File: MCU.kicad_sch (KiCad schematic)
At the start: 6 parts, among them U2 STM32G431CBU6, U3 TCAN337, Y1 ECS-80-20-5PX-TR

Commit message: MCU schematics update
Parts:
- removed U3: TCAN337, symbol Interface_CAN_LIN:TCAN337
- added C18, C19: 33pF, symbol Device:C_Small
- added C20: 100nF, Capacitor_SMD:C_0402_1005Metric, symbol Device:C_Small
- added C21: 1uF, Capacitor_SMD:C_0603_1608Metric, symbol Device:C
- added C22, C36: 4u7, Capacitor_SMD:C_0603_1608Metric, symbol Device:C_Small
- added C23, C24, C25, C26, C27, C32, C35, C37, C38, C39: 100n, Capacitor_SMD:C_0402_1005Metric, symbol Device:C_Small
- added C28, C42: 1u, Capacitor_SMD:C_0402_1005Metric, symbol Device:C_Small
- added C29, C43: 10n, Capacitor_SMD:C_0402_1005Metric, symbol Device:C_Small
- added C30, C31: 12p, Capacitor_SMD:C_0402_1005Metric, symbol Device:C_Small
- added C33, C34: 2u2, Capacitor_SMD:C_0603_1608Metric, symbol Device:C_Small
- added D9: ESD7104MUTAG, ESD8104MUTAG, symbol ESD7104MUTAG:ESD7104MUTAG
- added IC3: TCAN330DCNT, lib:SOT65P280X145-8N, symbol lib:TCAN330DCNT
- added J1: SM04B-GHS-TB, lib:CONN_SM04B-GHS-TB_JST, symbol lib:SM04B-GHS-TB
- added J2: Conn_01x04_Pin, Connector_PinHeader_1.00mm:PinHeader_1x04_P1.00mm_Vertical, symbol Connector:Conn_01x04_Pin
- added J3: USB_C_Receptacle_USB2.0_16P, Connector_USB:USB_C_Receptacle_GCT_USB4105-xx-A_16P_TopMnt_Horizontal, symbol Connector:USB_C_Receptacle_USB2.0_16P
- added L2: 39n, Inductor_SMD:L_0402_1005Metric, symbol Device:L_Small
- added L3: 100MHz / 1kR, Inductor_SMD:L_0402_1005Metric, symbol Device:L_Small
- added R18, R20: 10k, Resistor_SMD:R_0402_1005Metric, symbol Device:R_Small
- added R19: 120R, Resistor_SMD:R_0402_1005Metric, symbol Device:R_Small
- added R21: 47, Resistor_SMD:R_0402_1005Metric, symbol Device:R_Small
- added R22, R23: 2k2, Resistor_SMD:R_0402_1005Metric, symbol Device:R_Small
- added SW1: SW_SPDT, Button_Switch_SMD:SW_SPDT_PCM12, symbol Switch:SW_SPDT
- added U7: STM32F407VGTx, Package_QFP:LQFP-100_14x14mm_P0.5mm, symbol MCU_ST_STM32F4:STM32F407VGTx
- added Y2: 16MHz, Crystal:Crystal_SMD_3225-4Pin_3.2x2.5mm, symbol Device:Crystal_GND24_Small
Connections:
- net VDD is gone; now on net +3.3V: U2.23 (VDD), U2.35 (VDD), U2.48 (VDD)
- net GND: now also U2.49 (VSS), C18.2, C19.2, C20.2, C21.2, C22.2, C23.2, C24.2, C25.2, C26.2, C27.2, C28.2, C29.2, C30.2, C31.2, C32.2, C33.2, C34.2, C35.2, C36.2, C37.2, C38.2, C39.2, C42.2, C43.2, D9.3 (GND_1), D9.8 (GND_2), IC3.2 (GND), J1.3, J1.4, J2.4 (Pin_4), J3.A1 (GND), J3.A12 (GND), J3.B1 (GND), J3.B12 (GND), J3.S1 (SHIELD), SW1.3 (C), U7.10 (VSS), U7.20 (VSSA), U7.27 (VSS), U7.74 (VSS), U7.99 (VSS), Y2.2, Y2.4
- net at Y1.1: now also U2.6 (PF1-OSC_OUT), C18.1
- net at Y1.2: now also U2.5 (PF0-OSC_IN), C19.1
- net +3.3V: now reaches U2.1 (VBAT)
- net +3.3V: now also C20.1, C22.1, C23.1, C24.1, C25.1, C26.1, C27.1, C36.1, C37.1, C38.1, C39.1, IC3.3 (VCC), J2.1 (Pin_1), L2.1, L3.1, R22.1, R23.1, SW1.1 (A), U7.100 (VDD), U7.11 (VDD), U7.19 (VDD), U7.28 (VDD), U7.50 (VDD), U7.6 (VBAT), U7.75 (VDD)
- net SENS3: now reaches U2.10 (PA2)
- net INLB: now reaches U2.17 (PB0)
- net INLC: now reaches U2.18 (PB1)
- net INLA: now reaches U2.2 (PC13)
- net +3.3VA: now reaches U2.20 (VREF+)
- net +3.3VA: now also U2.21 (VDDA), C28.1, C29.1, C32.1, C35.1, C42.1, C43.1, L2.2, L3.2, U7.21 (VREF+), U7.22 (VDDA)
- net INHA: now reaches U2.30 (PA8)
- net INHB: now reaches U2.31 (PA9)
- net INHC: now reaches U2.32 (PA10)
- net USB_DN: now reaches U2.33 (PA11)
- net USB_DN: now also D9.2 (IO_2), D9.6 (NC_1), J3.A7 (D-), J3.B7 (D-)
- net USB_DP: now reaches U2.34 (PA12)
- net USB_DP: now also D9.1 (IO_1), D9.7 (NC_2), J3.A6 (D+), J3.B6 (D+)
- net SWDIO: now reaches U2.36 (PA13)
- net SWDIO: now also J2.2 (Pin_2), U7.72 (PA13)
- net SWCLK: now reaches U2.37 (PA14)
- net SWCLK: now also J2.3 (Pin_3), U7.76 (PA14)
- net UART_N: now reaches U2.39 (PC10)
- net UART_N: now also IC3.4 (RXD)
- net UART_P: now reaches U2.40 (PC11)
- net UART_P: now also IC3.1 (TXD)
- net BOOT0: now reaches U2.46 (PB8-BOOT0)
- net BOOT0: now also R20.2, U7.94 (BOOT0)
- net SENS1: now reaches U2.8 (PA0)
- net SENS2: now reaches U2.9 (PA1)
- new net: R20.1, SW1.2 (B)
- new net: IC3.6 (CANL), J1.1, R19.1
- new net: IC3.7 (CANH), J1.2, R19.2
- new net: C34.1, U7.49 (VCAP_1)
- new net: C33.1, U7.73 (VCAP_2)
- new net: IC3.5 (SHDN), R18.1
- new net: C31.1, R21.2, Y2.3
- new net BLUE_LED: U7.29 (PA4)
- new net GREEN_LED: U7.26 (PA3)
- new net HSE_IN: C30.1, U7.12 (PH0), Y2.1
- new net HSE_OUT: R21.1, U7.13 (PH1)
- new net I2C1_SCL: R22.2, U7.63 (PC6)
- new net I2C1_SDA: R23.2, U7.64 (PC7)
- new net NRST: U7.14 (NRST)
- new net PD2: IC3.8 (S), R18.2
- new net RED_LED: U7.25 (PA2)
- new net SWO: U7.89 (PB3)
- new net USART3_RX: U7.79 (PC11)
- new net USART3_TX: U7.78 (PC10)
- new net USB_D+: U7.71 (PA12)
- new net USB_D-: U7.70 (PA11)
- new net VBUS: C21.1, D9.4 (IO_3), D9.9 (NC_3), J3.A4 (VBUS), J3.A9 (VBUS), J3.B4 (VBUS), J3.B9 (VBUS)
- no-connect marks 0 -> 40
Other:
- note added: "Cload = 2 * (CL - Cstray)"
- note added: "STM32 Microcontroller"
- note added: "a 16 MHz crystal is perfectly fine for an STM32F407 and for USB Full-Speed, as long as you run the PLL to generate the 48 MHz USB clock and a stable SYSCLK."
- note added: "https://jlcpcb.com/partdetail/Korean_HropartsElec-TF01A/C91145"
- moved on the sheet: Y1

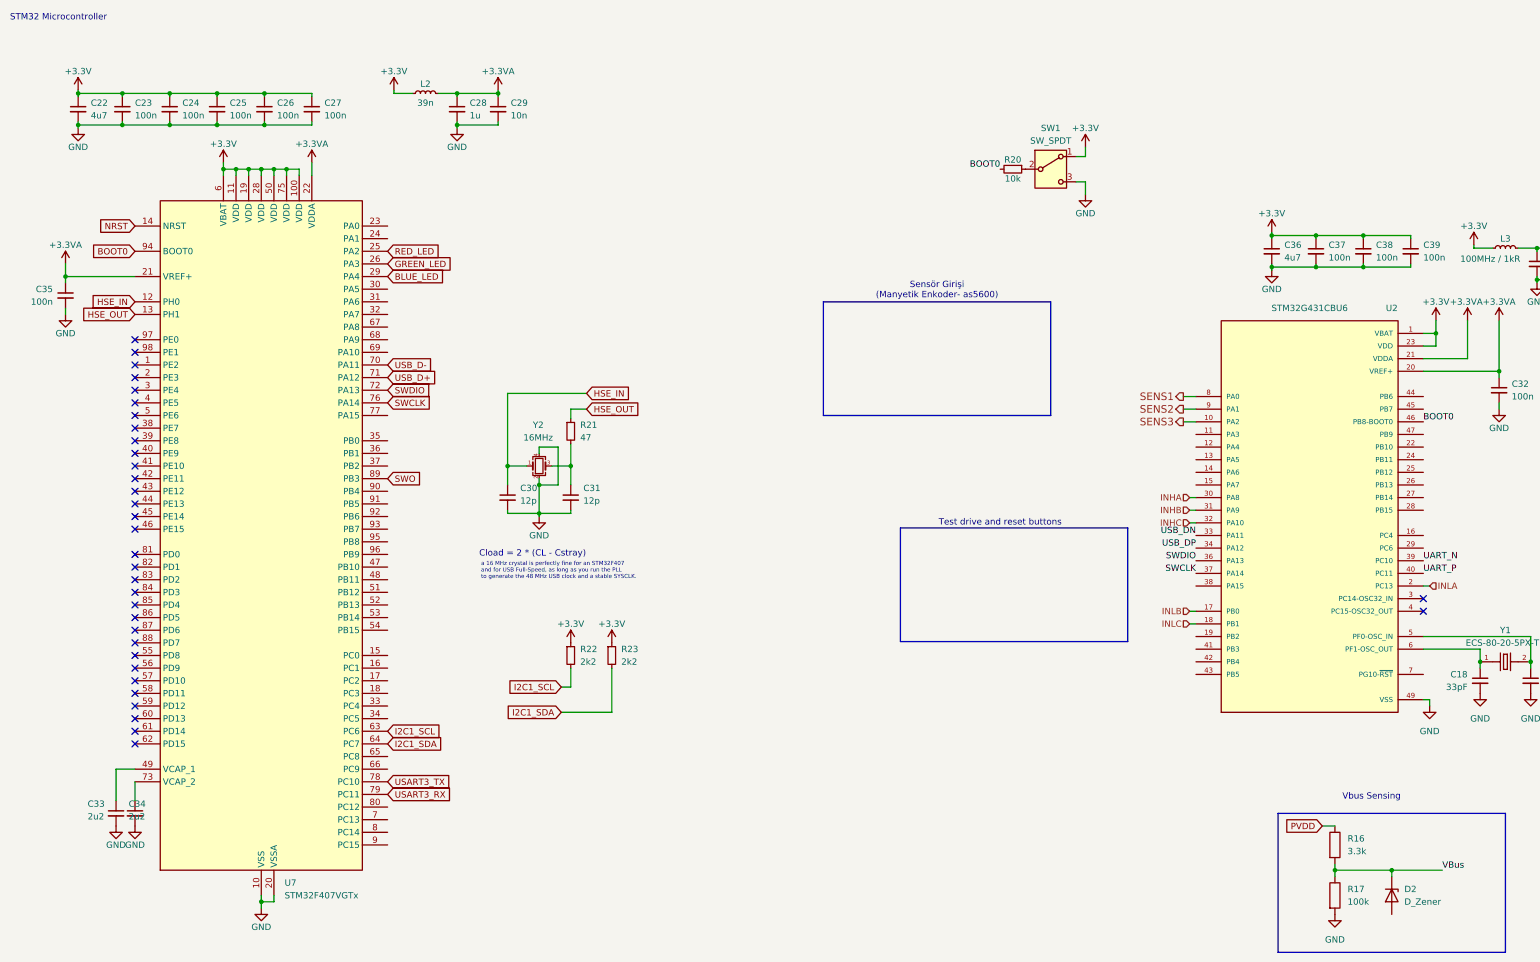
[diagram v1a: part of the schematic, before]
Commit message: MCU schematics update
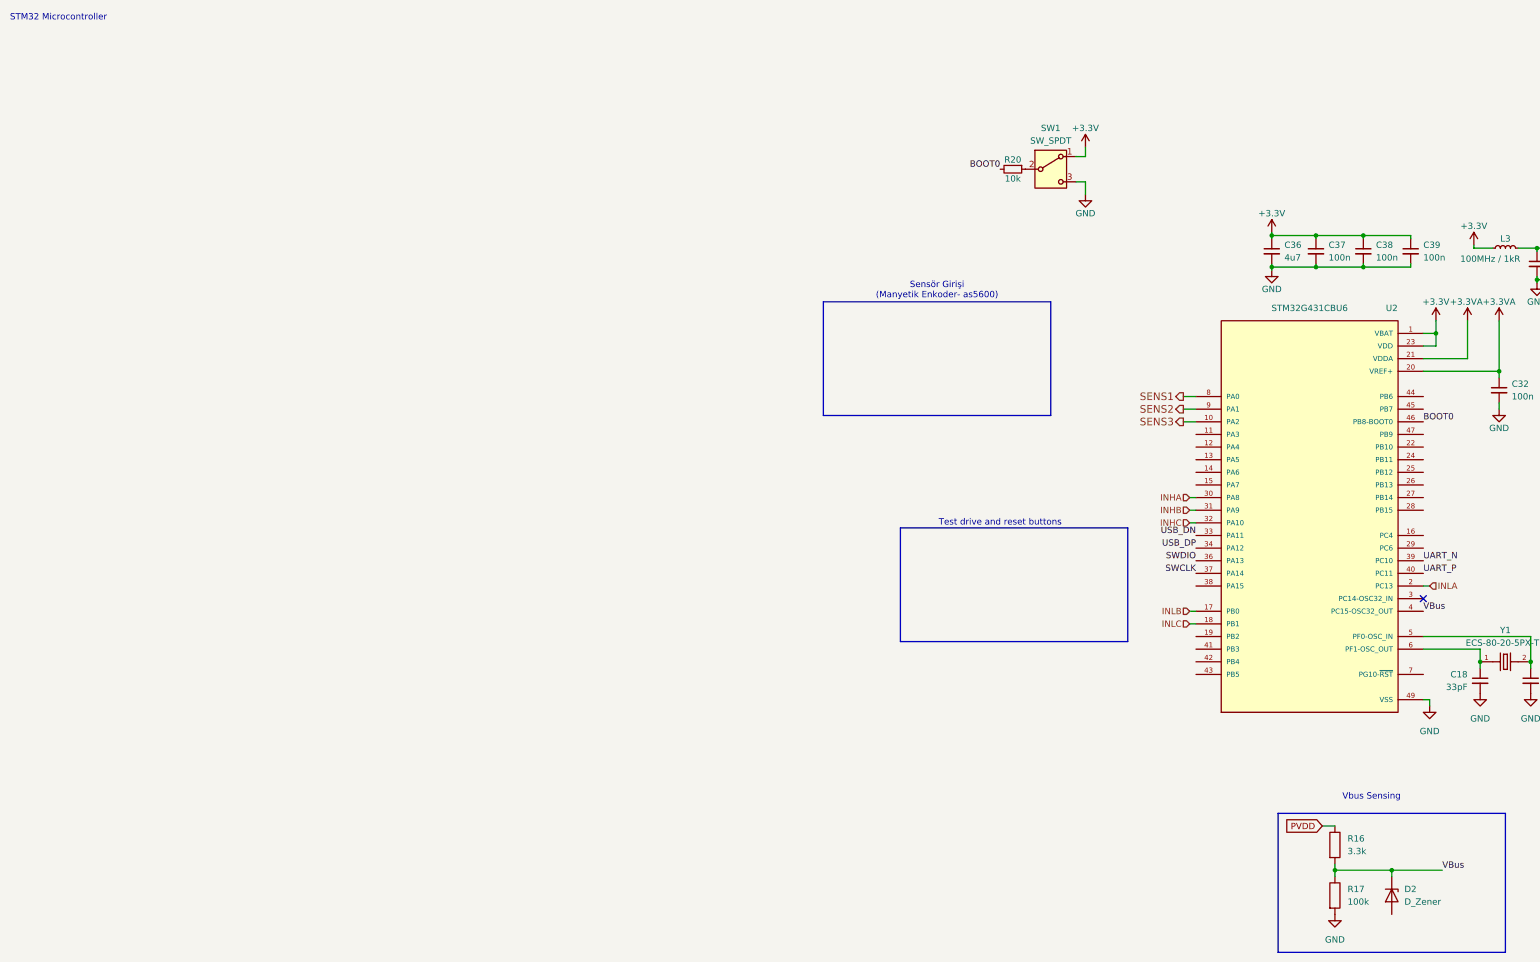
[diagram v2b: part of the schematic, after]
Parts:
- removed C22: 4u7, Capacitor_SMD:C_0603_1608Metric, symbol Device:C_Small
- removed C23, C24, C25, C26, C27, C35: 100n, Capacitor_SMD:C_0402_1005Metric, symbol Device:C_Small
- removed C28: 1u, Capacitor_SMD:C_0402_1005Metric, symbol Device:C_Small
- removed C29: 10n, Capacitor_SMD:C_0402_1005Metric, symbol Device:C_Small
- removed C30, C31: 12p, Capacitor_SMD:C_0402_1005Metric, symbol Device:C_Small
- removed C33, C34: 2u2, Capacitor_SMD:C_0603_1608Metric, symbol Device:C_Small
- removed L2: 39n, Inductor_SMD:L_0402_1005Metric, symbol Device:L_Small
- removed R21: 47, Resistor_SMD:R_0402_1005Metric, symbol Device:R_Small
- removed R22, R23: 2k2, Resistor_SMD:R_0402_1005Metric, symbol Device:R_Small
- removed U7: STM32F407VGTx, Package_QFP:LQFP-100_14x14mm_P0.5mm, symbol MCU_ST_STM32F4:STM32F407VGTx
- removed Y2: 16MHz, Crystal:Crystal_SMD_3225-4Pin_3.2x2.5mm, symbol Device:Crystal_GND24_Small
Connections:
- net VBus: now also U2.4 (PC15-OSC32_OUT)
- no-connect marks 40 -> 7
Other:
- note removed: "Cload = 2 * (CL - Cstray)"
- note removed: "a 16 MHz crystal is perfectly fine for an STM32F407 and for USB Full-Speed, as long as you run the PLL to generate the 48 MHz USB clock and a stable SYSCLK."

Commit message: whakkjls
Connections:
- net GND: now also D2.2 (A)
- net VBus: now also U2.19 (PB2); no longer U2.4 (PC15-OSC32_OUT)
- net I2C1_SCL: now reaches U2.38 (PA15)
- net I2C1_SDA: now reaches U2.45 (PB7)
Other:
- moved on the sheet: D2, J2, R16, R17, R20, SW1

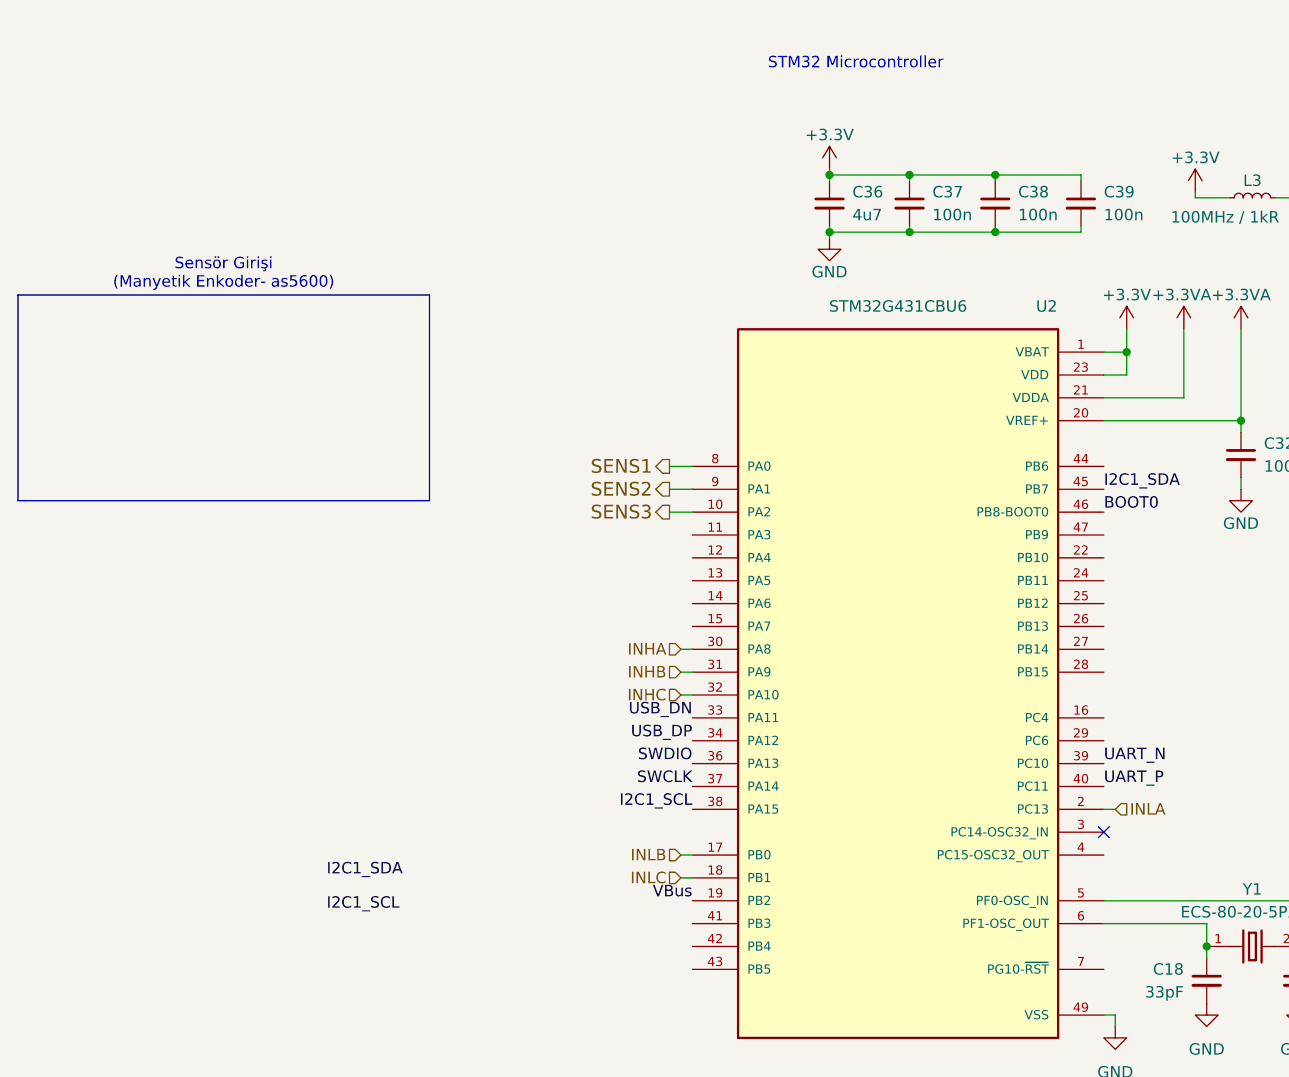
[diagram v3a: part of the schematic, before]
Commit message: some pins changes"
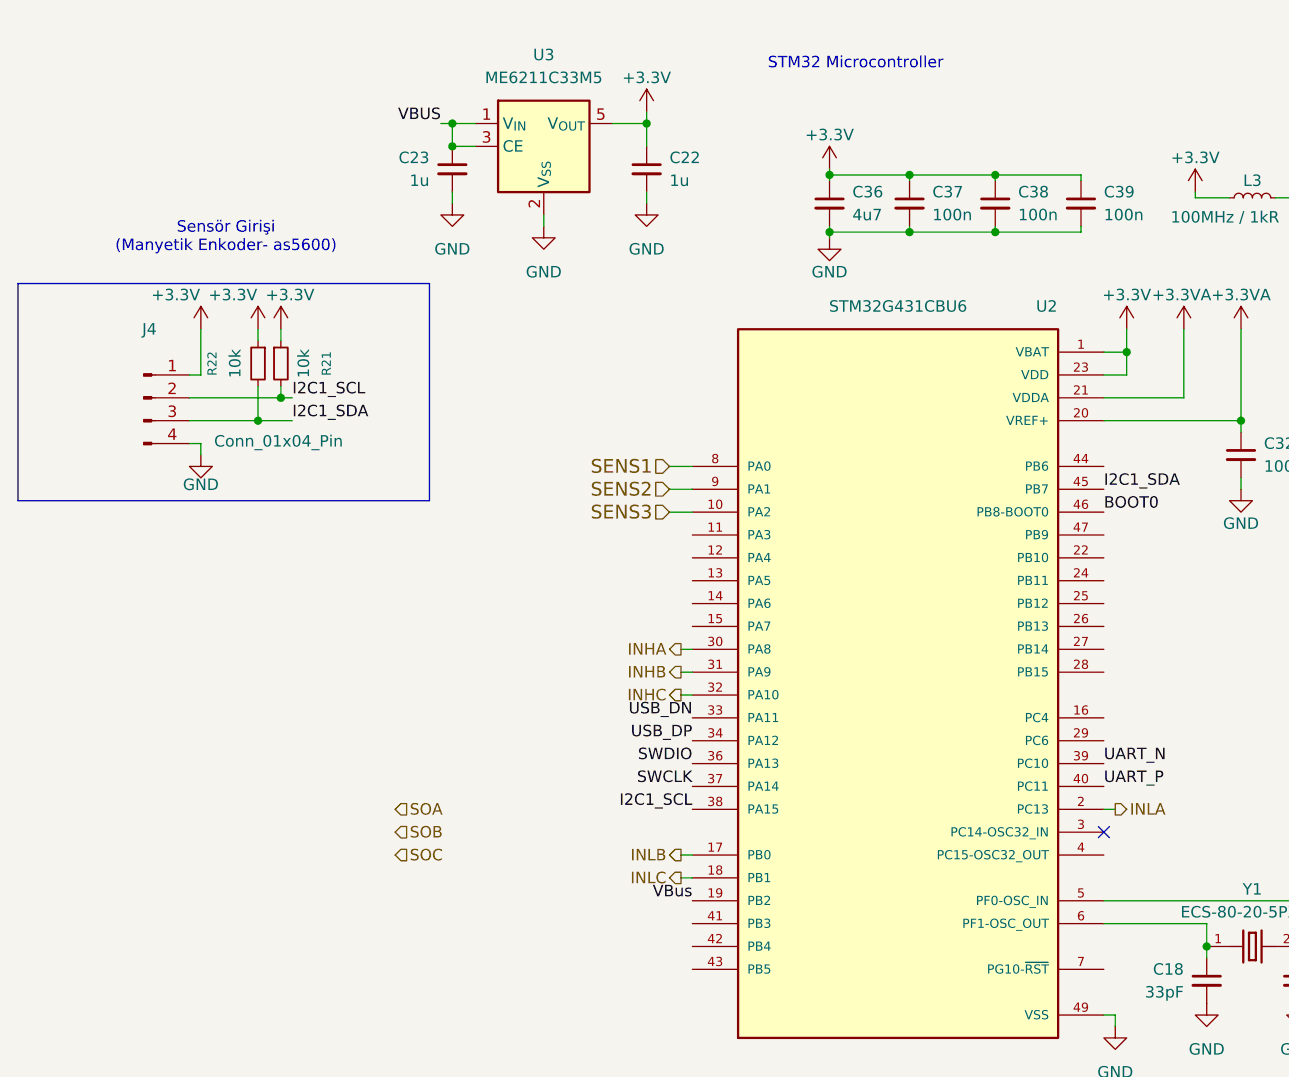
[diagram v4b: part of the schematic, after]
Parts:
- added C22, C23: 1u, Capacitor_SMD:C_0402_1005Metric, symbol Device:C_Small
- added J4: Conn_01x04_Pin, symbol Connector:Conn_01x04_Pin
- added R21, R22: 10k, Resistor_SMD:R_0402_1005Metric, symbol Device:R_Small
- added U3: ME6211C33M5, Package_TO_SOT_SMD:SOT-23-5, symbol Regulator_Linear:ME6211C33M5
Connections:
- net +3.3V: now also C22.1, J4.1 (Pin_1), R21.1, R22.1, U3.5 (V_{OUT})
- net GND: now also C22.2, C23.2, J4.4 (Pin_4), U3.2 (V_{SS})
- net I2C1_SCL: now also J4.2 (Pin_2), R21.2
- net I2C1_SDA: now also J4.3 (Pin_3), R22.2
- net VBUS: now also C23.1, U3.1 (V_{IN}), U3.3 (CE)

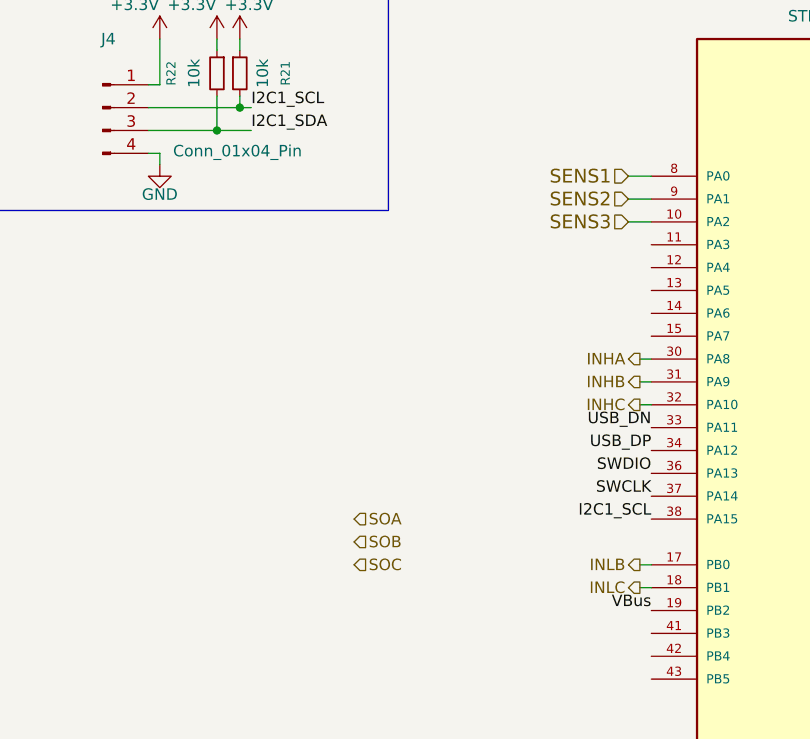
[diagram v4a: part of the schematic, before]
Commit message: current sense -> bemf switch
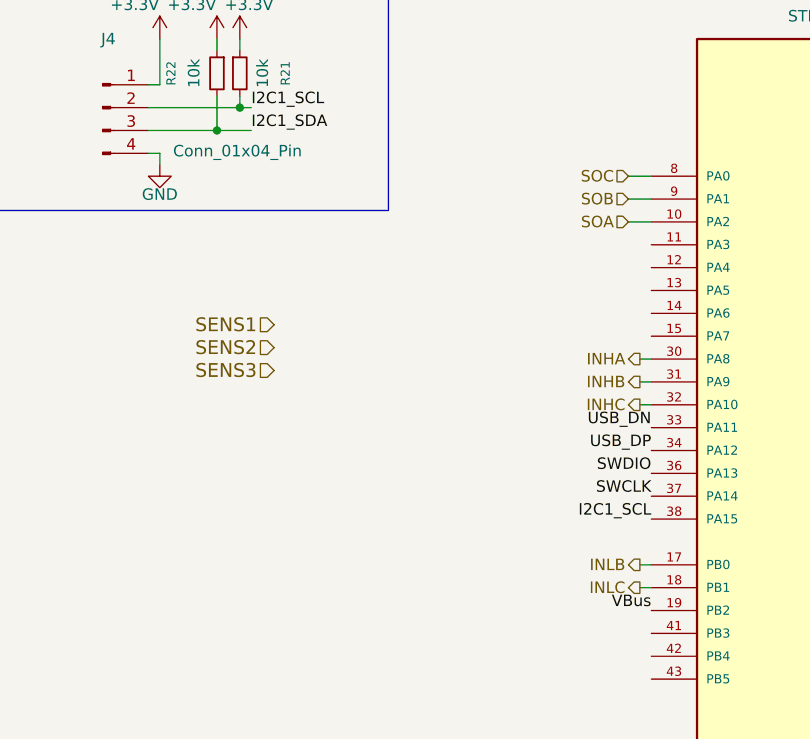
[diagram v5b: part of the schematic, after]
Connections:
- net SENS1: no longer U2.8 (PA0)
- net SENS2: no longer U2.9 (PA1)
- net SENS3: no longer U2.10 (PA2)
- net SOA: now also U2.10 (PA2)
- net SOB: now also U2.9 (PA1)
- net SOC: now also U2.8 (PA0)
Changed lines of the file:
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@@
+		)
+	)
+	(hierarchical_label "SENS3"
+		(shape input)
+		(at 67.31 88.9 180)
+		(effects
+			(font
+				(size 1.524 1.524)
+			)
+			(justify right)
 		)
 	)
@@
 		)
 	)
-	(hierarchical_label "SENS2"
+	(hierarchical_label "SOB"
 		(shape input)
 		(at 106.68 69.85 180)
 		(effects
 			(font
-				(size 1.524 1.524)
+				(size 1.27 1.27)
 			)
 			(justify right)
@@
 	(hierarchical_label "SENS1"
 		(shape input)
-		(at 106.68 67.31 180)
+		(at 67.31 83.82 180)
 		(effects
 			(font
@@
 			)
 			(justify right)
-		)
-	)
-	(hierarchical_label "SOB"
-		(shape input)
-		(at 76.2 107.95 0)
-		(effects
-			(font
-				(size 1.27 1.27)
-			)
-			(justify left)
 		)
 	)
@@
 	(hierarchical_label "SOA"
 		(shape input)
-		(at 76.2 105.41 0)
+		(at 106.68 72.39 180)
 		(effects
 			(font
 				(size 1.27 1.27)
 			)
-			(justify left)
+			(justify right)
 		)
 	)
@@
 	(hierarchical_label "SOC"
 		(shape input)
-		(at 76.2 110.49 0)
+		(at 106.68 67.31 180)
 		(effects
 			(font
 				(size 1.27 1.27)
 			)
-			(justify left)
+			(justify right)
 		)
 	)
-	(hierarchical_label "SENS3"
+	(hierarchical_label "SENS2"
 		(shape input)
-		(at 106.68 72.39 180)
+		(at 67.31 86.36 180)
 		(effects
 			(font
